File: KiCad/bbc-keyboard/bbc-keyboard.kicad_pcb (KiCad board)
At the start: 2 copper layers, 337.8 x 137.2 mm, 101 parts, among them IC1 74LS161, IC2 74251, IC3 74145, IC4 74LS30, SW1 escape, SW10 W, SW11 2, SW12 A, SW13 S, SW14 Z, SW15 f2, SW16 4, SW17 E, SW18 D, SW19 X, SW2 Q, SW20 C, SW21 space, SW22 f3, SW23 5, SW24 T, SW25 R, SW26 F, SW27 G, SW28 V, SW29 f5, SW3 F0, SW30 F4, SW31 7, SW32 6, SW33 Y, SW34 H, SW35 B, SW36 f6, SW37 8, SW38 9, SW39 U, SW4 1, SW40 J, SW41 N, SW42 M, SW43 f8, SW44 f7, SW45 I, SW46 O, SW47 K, SW48 L, SW49 <,, SW5 caps lk, SW50 f9, SW51 =-, SW52 0, SW53 P, SW54 @, SW55 ;+, SW56 >., SW57 \|, SW58 ~^, SW59 _£, SW6 shift lk, SW60 {[, SW61 *:, SW62 }], SW63 ?/, SW64 right, SW65 left, SW66 down, SW67 up, SW68 return, SW69 delete, SW7 tab, SW70 copy, SW71 shift, SW72 shift, SW73 ctrl, SW74 SW_DIP_x08, SW75 break, SW8 f1, SW9 3

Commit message: more layout tidying
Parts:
- moved D3 6.35 mm to (322.9, 209.6)
- moved D6 6.35 mm to (315.3, 209.6)
- moved D10 6.35 mm to (305.1, 209.6)
- moved D4 6.35 mm to (320.4, 209.6)
- moved D5 6.35 mm to (317.8, 209.6)
- moved D7 6.35 mm to (312.7, 209.6)
- moved D8 6.35 mm to (310.2, 209.6)
- moved D9 6.35 mm to (307.7, 209.6)
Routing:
- net /Key Matrix/KC_COL2: track 472.7 -> 463.8 mm
- net /Key Matrix/KC_COL9: track 221.6 -> 228.2 mm
- net /Key Matrix/KC_COL5: track 345.4 -> 341.4 mm
- net /Key Matrix/KC_COL8: track 207.2 -> 204.4 mm
- net /Key Matrix/KC_COL3: track 453.8 -> 451.1 mm
- net /Key Matrix/KC_COL4: track 391.7 -> 389.3 mm
- net /Key Matrix/KC_COL6: track 297.3 -> 295.1 mm
- net Net-(D10-Pad2): track 46.6 -> 44.9 mm
- net /Key Matrix/KC_COL7: track 250.3 -> 248.8 mm
- net Net-(D9-Pad2): track 40.7 -> 39.3 mm
- net Net-(D3-Pad2): track 3.81 -> 5.09 mm
- net Net-(D8-Pad2): track 34.8 -> 33.8 mm
- net Net-(D7-Pad2): track 29.0 -> 28.2 mm

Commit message: DRC pass
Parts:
- PL1: footprint Connector_PinHeader_2.54mm:PinHeader_1x17_P2.54mm_Horizontal -> SpecialConnectors:PinHeader_1x17_P2.54mm_Horizontal_noSilk
- moved C4 95.5 mm to (223.1, 100.3)
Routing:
- net /Key Matrix/KC_ROW0: track 451.5 -> 658.2 mm
- net /Key Matrix/KC_ROW5: track 471.4 -> 623.5 mm
- net /Key Matrix/KC_ROW4: track 571.9 -> 693.5 mm
- net /Key Matrix/KC_ROW6: track 530.5 -> 634.7 mm
- net /Key Matrix/KC_ROW3: track 559.9 -> 624.1 mm
- net /Key Matrix/KC_ROW7: track 442.5 -> 491.2 mm, vias 0 -> 1
- net /Key Matrix/KC_ROW1: track 435.2 -> 470.9 mm
- net /Key Matrix/KC_ROW2: track 428.6 -> 462.6 mm
- net /Key Matrix/KC_COL1: track 336.5 -> 331.8 mm, vias 1 -> 0
- net VCC: track 592.0 -> 595.6 mm
- net GND: track 289.8 -> 291.9 mm
- net Net-(LD3-Pad1): track 176.2 -> 174.7 mm
- net Net-(LD2-Pad1): track 180.0 -> 181.1 mm
- net /CA2: track 180.7 -> 180.1 mm

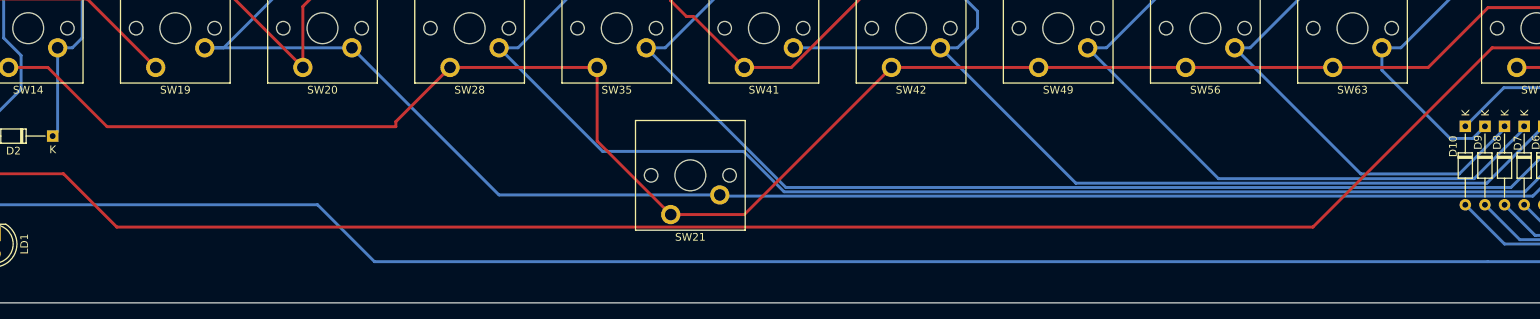
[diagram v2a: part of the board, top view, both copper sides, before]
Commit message: Add stabilizer for space
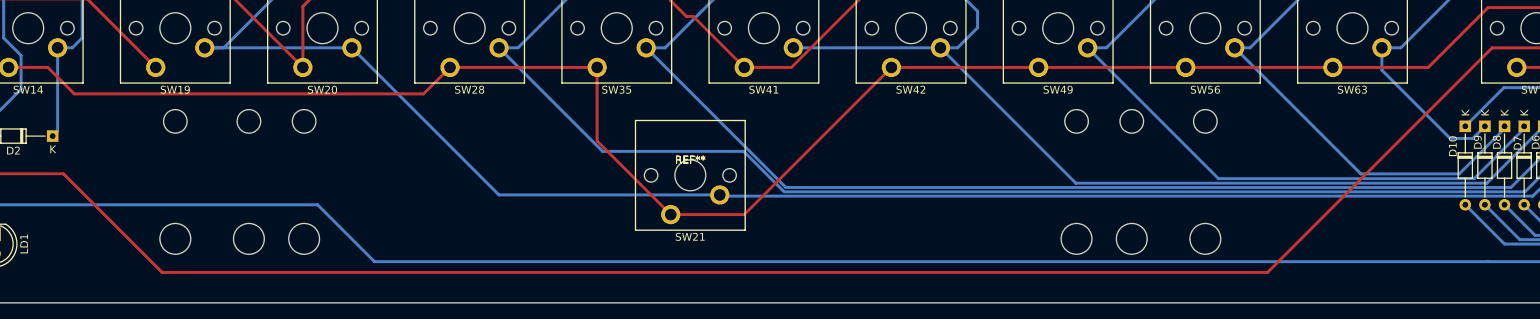
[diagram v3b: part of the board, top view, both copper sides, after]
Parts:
- added REF**: Stabilizer_Cherry_MX_6.25u, Mounting_Keyboard_Stabilizer:Stabilizer_Cherry_MX_6.25u, F.Cu at (204.8, 215.9)
- added REF**: Stabilizer_Cherry_MX_7.00u, Mounting_Keyboard_Stabilizer:Stabilizer_Cherry_MX_7.00u, F.Cu at (204.8, 215.9)
- added REF**: Stabilizer_Cherry_MX_8.00u, Mounting_Keyboard_Stabilizer:Stabilizer_Cherry_MX_8.00u, F.Cu at (204.8, 215.9)
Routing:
- net Net-(D1-Pad2): track 266.6 -> 271.5 mm
- net /Key Matrix/KC_ROW6: track 634.7 -> 630.8 mm
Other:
- board text added: "6.25u, 7u, 8u PCB mount stabilizers not 6.5u For 6.25, 6.5u, 7u, 8u spacebar use cutouts"

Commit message: return stabilizers
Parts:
- added REF**: Stabilizer_Cherry_MX_2.00u, Mounting_Keyboard_Stabilizer:Stabilizer_Cherry_MX_2.00u, F.Cu at (347.7, 177.8)

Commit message: mounting holes for backplates
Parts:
- added J1: bkplt, MountingHole:MountingHole_2.7mm_M2.5_DIN965_Pad, F.Cu at (51.1, 132.1)
- added J2: bkplt, MountingHole:MountingHole_2.7mm_M2.5_DIN965_Pad, F.Cu at (51.1, 227.3)
- added J3: bkplt, MountingHole:MountingHole_2.7mm_M2.5_DIN965_Pad, F.Cu at (58.7, 176.5)
- added J4: bkplt, MountingHole:MountingHole_2.7mm_M2.5_DIN965_Pad, F.Cu at (378.8, 132.1)
- added J5: bkplt, MountingHole:MountingHole_2.7mm_M2.5_DIN965_Pad, F.Cu at (378.8, 176.5)
- added J6: bkplt, MountingHole:MountingHole_2.7mm_M2.5_DIN965_Pad, F.Cu at (363.5, 227.3)
- moved RP1 1.80 mm to (373.7, 137.2)
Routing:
- net GND: track 291.9 -> 958.4 mm
- net VCC: track 595.6 -> 591.4 mm
- net /Key Matrix/KC_ROW0: track 658.2 -> 654.8 mm
- net /Key Matrix/KC_ROW6: track 631.3 -> 628.2 mm
- net /Key Matrix/KC_ROW3: track 623.7 -> 621.0 mm
- net /Key Matrix/KC_ROW4: track 693.1 -> 690.5 mm
- net /Key Matrix/KC_ROW5: track 623.1 -> 620.5 mm
- net Net-(LD2-Pad1): track 181.1 -> 180.2 mm
- net Net-(LD1-Pad1): track 206.5 -> 207.0 mm

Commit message: mounting holes
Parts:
- removed J1, J2, J3, J4, J5, J6: bkplt, MountingHole:MountingHole_2.7mm_M2.5_DIN965_Pad
- added H1: bkplt, MountingHole:MountingHole_2.7mm_M2.5_DIN965_Pad, F.Cu at (51.1, 132.1)
- added H10: HoleThru, MountingHole:MountingHole_6.5mm, F.Cu at (-21.4, 115.9)
- added H11: HoleThru, MountingHole:MountingHole_6.5mm, F.Cu at (-36.0, 101.4)
- added H12: HoleThru, MountingHole:MountingHole_6.5mm, F.Cu at (-50.5, 115.9)
- added H13: HoleThru, MountingHole:MountingHole_6.5mm, F.Cu at (-50.5, 101.4)
- added H14: HoleThru, MountingHole:MountingHole_6.5mm, F.Cu at (-36.0, 115.9)
- added H15: front, MountingHole:MountingHole_2.7mm_M2.5_DIN965_Pad, F.Cu at (63.8, 217.2)
- added H16: front, MountingHole:MountingHole_2.7mm_M2.5_DIN965_Pad, F.Cu at (7.84, 101.5)
- added H17: front, MountingHole:MountingHole_2.7mm_M2.5_DIN965_Pad, F.Cu at (7.84, 95.2)
- added H18: front, MountingHole:MountingHole_2.7mm_M2.5_DIN965_Pad, F.Cu at (1.59, 101.5)
- added H2: bkplt, MountingHole:MountingHole_2.7mm_M2.5_DIN965_Pad, F.Cu at (51.1, 227.3)
- added H3: bkplt, MountingHole:MountingHole_2.7mm_M2.5_DIN965_Pad, F.Cu at (58.7, 176.5)
- added H4: bkplt, MountingHole:MountingHole_2.7mm_M2.5_DIN965_Pad, F.Cu at (378.8, 132.1)
- added H5: bkplt, MountingHole:MountingHole_2.7mm_M2.5_DIN965_Pad, F.Cu at (378.8, 176.5)
- added H6: bkplt, MountingHole:MountingHole_2.7mm_M2.5_DIN965_Pad, F.Cu at (363.5, 227.3)
- added H7: front, MountingHole:MountingHole_2.7mm_M2.5_DIN965_Pad, F.Cu at (101.9, 100.3)
- added H8: front, MountingHole:MountingHole_2.7mm_M2.5_DIN965_Pad, F.Cu at (63.8, 142.2)
- added H9: HoleThru, MountingHole:MountingHole_6.5mm, F.Cu at (-21.4, 101.4)
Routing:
- net GND: track 958.4 -> 1143.7 mm, vias 0 -> 1
- net /Key Matrix/KC_ROW6: track 628.2 -> 618.4 mm
- net VCC: track 591.4 -> 583.4 mm

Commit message: mounting holes
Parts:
- H10, H11, H12, H13, H14, H9: footprint MountingHole:MountingHole_6.5mm -> Holes:SquareHole_6.5mm
- moved H9 375.2 mm to (353.4, 118.1)
- moved H12 361.2 mm to (302.6, 191.8)
- moved H16 334.5 mm to (341.9, 118.1)
- moved H10 282.9 mm to (244.2, 213.4)
- moved H18 248.8 mm to (223.8, 213.4)
- moved H11 230.4 mm to (165.4, 213.4)
- moved H17 213.5 mm to (185.7, 213.4)
- moved H13 181.6 mm to (107.0, 191.8)
- moved H14 103.9 mm to (63.8, 144.8)
- moved H2 10.2 mm to (51.1, 217.2)
- moved H1 10.2 mm to (51.1, 142.2)
- moved H8 10.2 mm to (63.8, 132.1)
- moved H15 7.62 mm to (63.8, 224.8)
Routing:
- net GND: track 1143.7 -> 1099.4 mm
- net VCC: track 583.4 -> 572.2 mm
- net /Key Matrix/KC_ROW4: track 690.5 -> 693.8 mm
- net Net-(LD3-Pad1): track 174.2 -> 171.9 mm
- net /Key Matrix/KC_ROW5: track 620.5 -> 618.5 mm
- net /Key Matrix/KC_COL8: track 204.4 -> 203.4 mm
